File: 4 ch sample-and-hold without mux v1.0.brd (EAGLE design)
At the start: 66 x 32.1 mm, 25 parts, among them IC5 TL074D

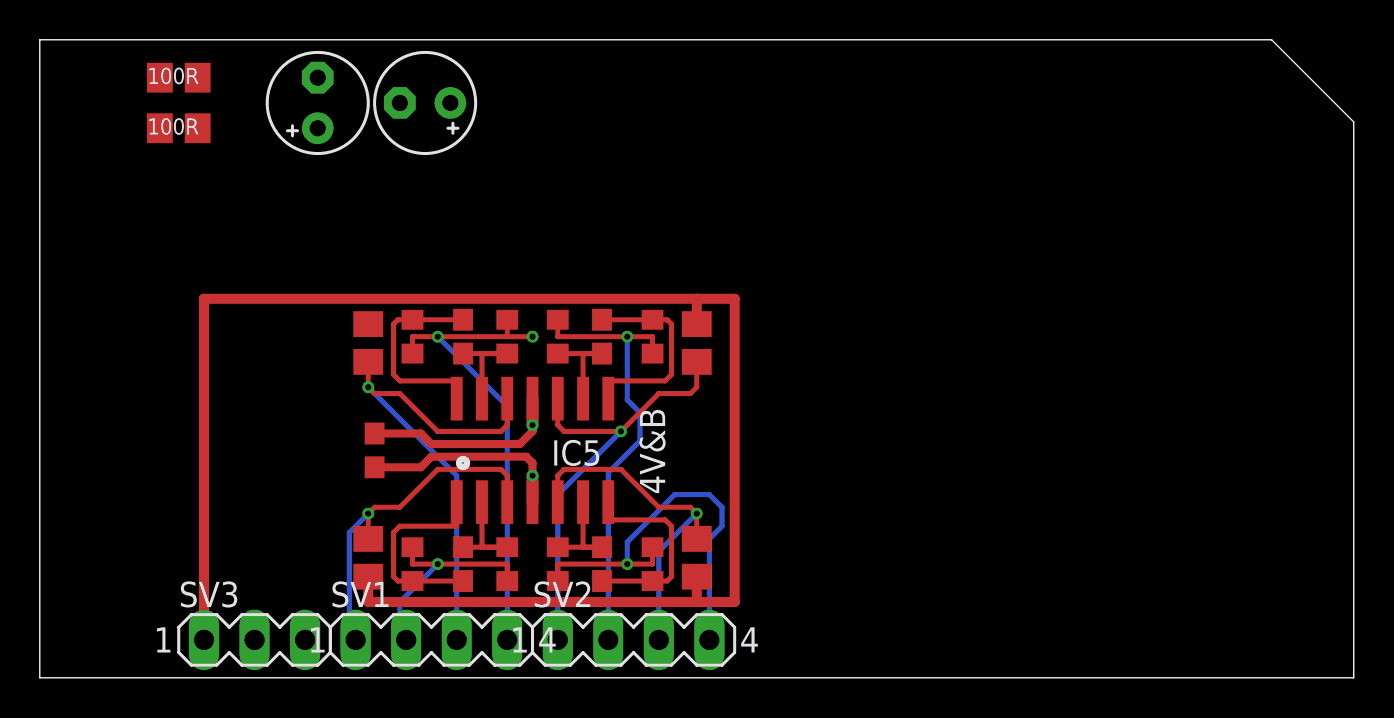
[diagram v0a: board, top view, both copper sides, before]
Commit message: Just missing logo
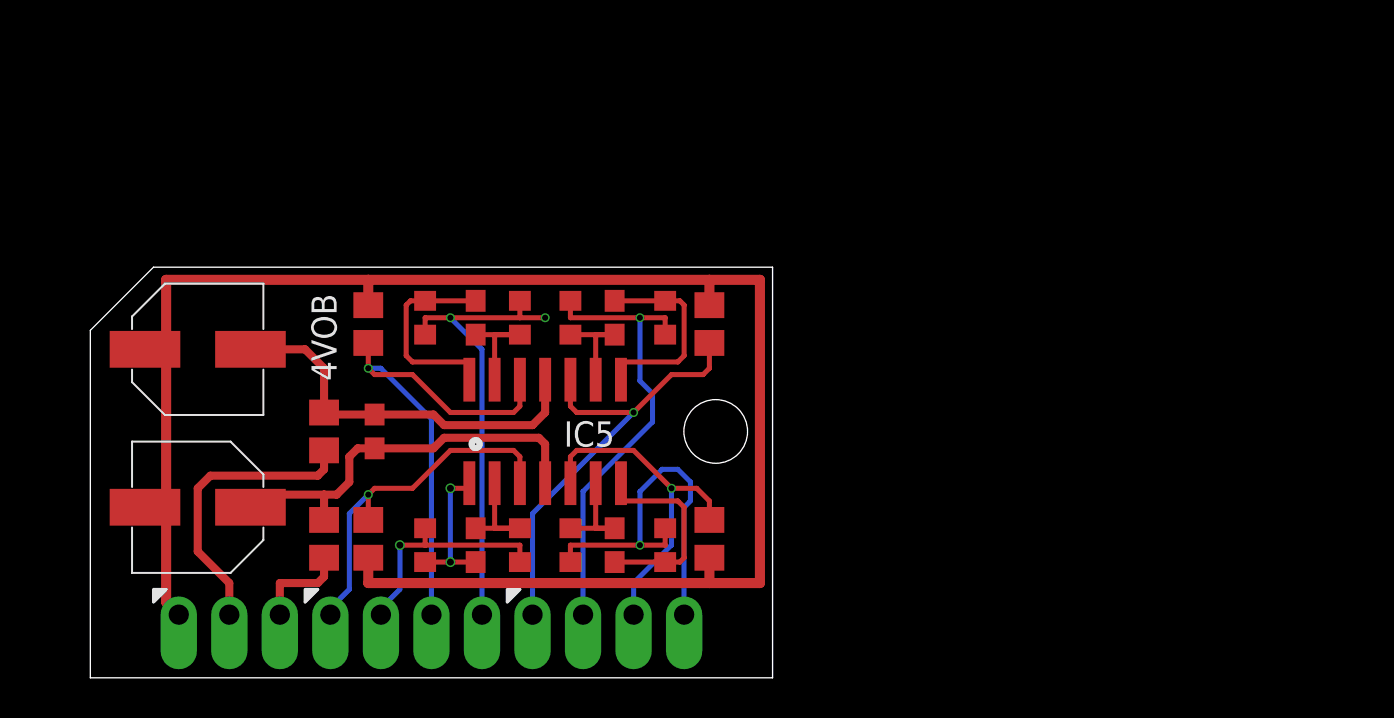
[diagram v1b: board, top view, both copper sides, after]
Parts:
- C2, C3: device resistor:E2,5-5 -> joakim-jclpcb:CAPAE660X610N
- SV1, SV2: device con-lstb:MA04-1 -> joakim:SIP-PIN04-1J
- SV3: device con-lstb:MA03-1 -> joakim:SIP-PIN03-1J
- moved R2 21.9 mm to (14.3, 6.99), turned to 270 degrees
- moved C3 21.2 mm to (7.94, 8.57), turned to 180 degrees
- moved R1 19.2 mm to (14.3, 12.4), turned to 270 degrees
- moved C2 16.9 mm to (7.94, 16.5), turned to 0 degrees
- moved SV1 1.80 mm to (18.4, 3.17)
- moved SV2 1.80 mm to (28.6, 3.17)
- moved SV3 1.80 mm to (9.53, 3.17)
- moved R29 1.14 mm to (26.7, 18.1)
- moved R30 1.14 mm to (31.4, 18.1)
- moved R31 1.14 mm to (26.7, 6.67)
- moved R32 1.14 mm to (31.4, 6.67)
- moved C27 1.14 mm to (33.7, 17.8)
- moved C28 1.14 mm to (33.7, 6.99)
- moved C36 1.14 mm to (21.9, 18.1)
- moved C37 1.14 mm to (28.9, 18.1)
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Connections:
- net +15V: now also C3.1; no longer C3.+
- net -15V: now also C2.2; no longer C2.-
- net AGND: now also C2.1, C3.2; no longer C2.+, C3.-
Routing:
- net V-: track 0.00 -> 14.7 mm
- net +15V: track 10.3 -> 20.4 mm, vias 1 -> 0
- net -15V: track 10.1 -> 19.6 mm, vias 1 -> 0
- net AGND: track 81.3 -> 89.1 mm
- net V+: track 0.00 -> 4.90 mm
- net N$33: track 10.3 -> 7.46 mm, vias 0 -> 2
- net OUT4: track 20.5 -> 19.2 mm
- net OUT2: track 24.4 -> 23.3 mm
- net IN1: track 17.5 -> 18.1 mm
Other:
- board size 66 x 32.1 mm -> 34.3 x 20.6 mm
- board text added: "2"
- board text added: "3"
- board text added: "4"
- board text added: "4VOB"
- board text added: "IN"
- board text added: "OUT"
- board text removed: "100R"
- board text removed: "4V&B"
- board text removed: "9"
- board text removed: "Outputs"

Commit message: Added logo
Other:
- board text added: "4 ch. CV buffer"

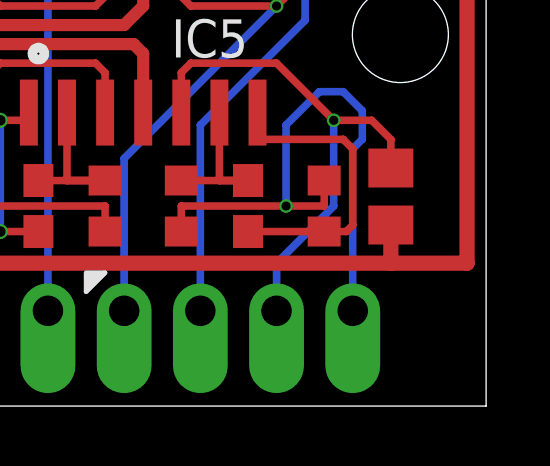
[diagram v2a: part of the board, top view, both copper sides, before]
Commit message: Created parts list, cleaned up schematics
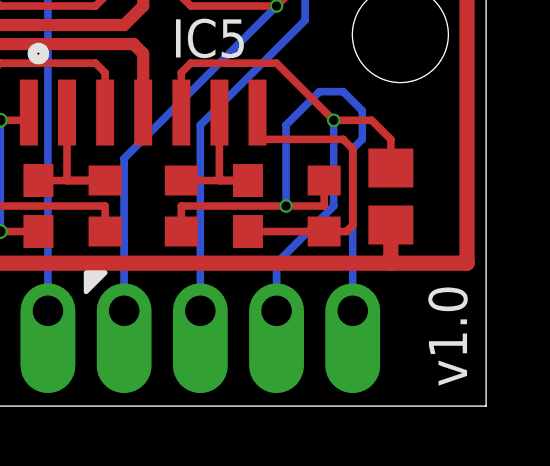
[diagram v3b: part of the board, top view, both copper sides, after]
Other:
- board text added: "v1.0"
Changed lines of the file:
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@@
 </polygon>
 <text x="31.115" y="12.3825" size="1.778" layer="26" font="vector" rot="MR0">4 ch. CV buffer</text>
+<text x="36.195" y="0.635" size="1.27" layer="25" ratio="16" rot="R90">v1.0</text>
 </plain>
 <attributes>

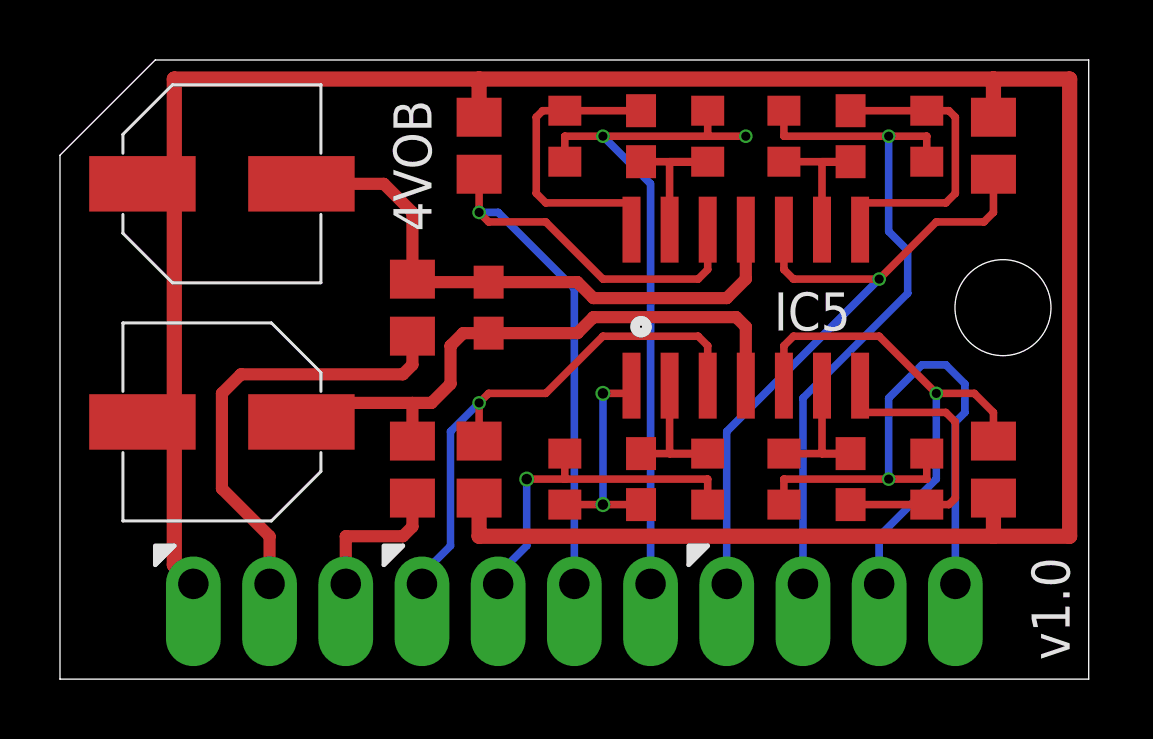
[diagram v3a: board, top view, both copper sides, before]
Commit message: Changed to logo-as-component
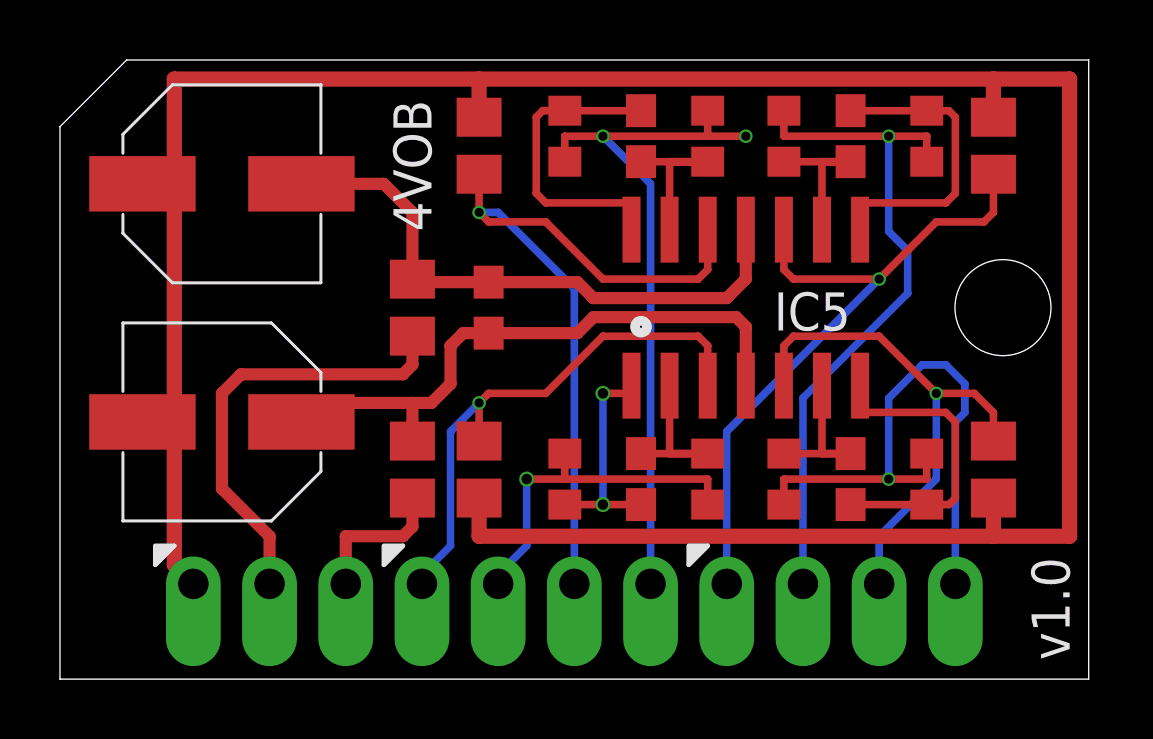
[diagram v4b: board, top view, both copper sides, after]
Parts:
- added U$1: (no value), joakim:XONIK_LOGO_20
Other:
- outline, holes or cut-outs redrawn

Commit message: changed from 0.1uF to 330pF to align with Fat Controller circuit
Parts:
- C36, C37, C38, C39: value 0.1uF -> 330pF
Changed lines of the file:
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@@
 <attribute name="VALUE" x="13.97" y="19.05" size="1.27" layer="27" rot="R270"/>
 </element>
-<element name="C39" library="resistor" package="C0603" value="0.1uF" x="21.9075" y="6.6675" smashed="yes" rot="R90">
+<element name="C39" library="resistor" package="C0603" value="330pF" x="21.9075" y="6.6675" smashed="yes" rot="R90">
 <attribute name="VALUE" x="23.8125" y="6.0325" size="1.27" layer="27" rot="R90"/>
 </element>
@@
 <attribute name="VALUE" x="24.765" y="7.3025" size="1.27" layer="27" rot="R270"/>
 </element>
-<element name="C38" library="resistor" package="C0603" value="0.1uF" x="28.8925" y="6.6675" smashed="yes" rot="R90">
+<element name="C38" library="resistor" package="C0603" value="330pF" x="28.8925" y="6.6675" smashed="yes" rot="R90">
 <attribute name="VALUE" x="30.7975" y="6.0325" size="1.27" layer="27" rot="R90"/>
 </element>
-<element name="C37" library="resistor" package="C0603" value="0.1uF" x="28.8925" y="18.0975" smashed="yes" rot="R270">
+<element name="C37" library="resistor" package="C0603" value="330pF" x="28.8925" y="18.0975" smashed="yes" rot="R270">
 <attribute name="VALUE" x="26.9875" y="18.7325" size="1.27" layer="27" rot="R270"/>
 </element>
@@
 <attribute name="VALUE" x="28.575" y="17.4625" size="1.27" layer="27" rot="R90"/>
 </element>
-<element name="C36" library="resistor" package="C0603" value="0.1uF" x="21.9075" y="18.0975" smashed="yes" rot="R270">
+<element name="C36" library="resistor" package="C0603" value="330pF" x="21.9075" y="18.0975" smashed="yes" rot="R270">
 <attribute name="VALUE" x="20.0025" y="18.7325" size="1.27" layer="27" rot="R270"/>
 </element>

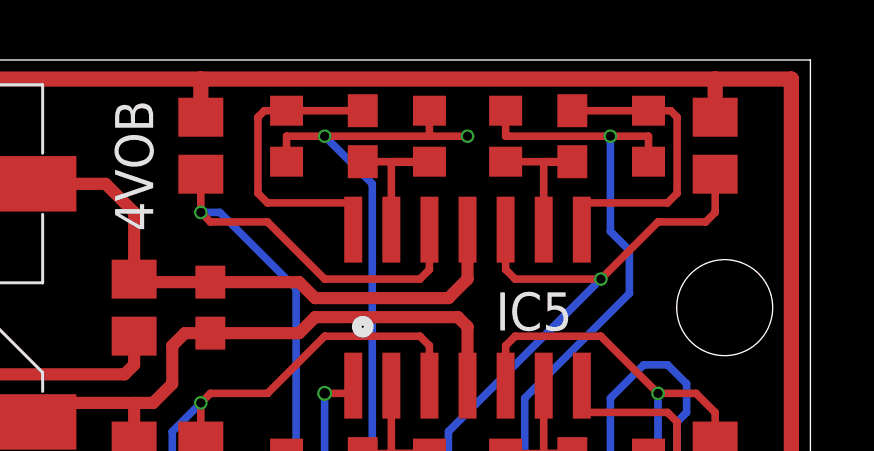
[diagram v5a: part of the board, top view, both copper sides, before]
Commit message: Fixed error in silk screen
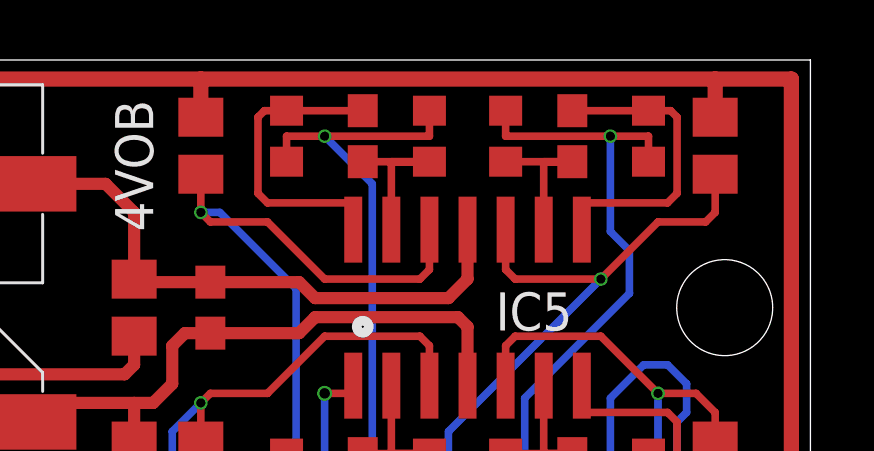
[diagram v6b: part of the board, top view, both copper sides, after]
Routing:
- net OUT2: track 23.3 -> 22.0 mm, vias 2 -> 1
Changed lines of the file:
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@@
 <wire x1="20.6375" y1="18.0975" x2="24.13" y2="18.0975" width="0.254" layer="1"/>
 <wire x1="24.13" y1="18.0975" x2="24.13" y2="18.9475" width="0.254" layer="1"/>
-<wire x1="24.13" y1="18.0975" x2="25.4" y2="18.0975" width="0.254" layer="1"/>
-<via x="25.4" y="18.0975" extent="1-16" drill="0.3048"/>
 <contactref element="SV1" pad="4"/>
 <wire x1="22.225" y1="16.51" x2="22.225" y2="3.175" width="0.254" layer="16"/>
